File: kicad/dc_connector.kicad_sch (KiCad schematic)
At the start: 8 parts

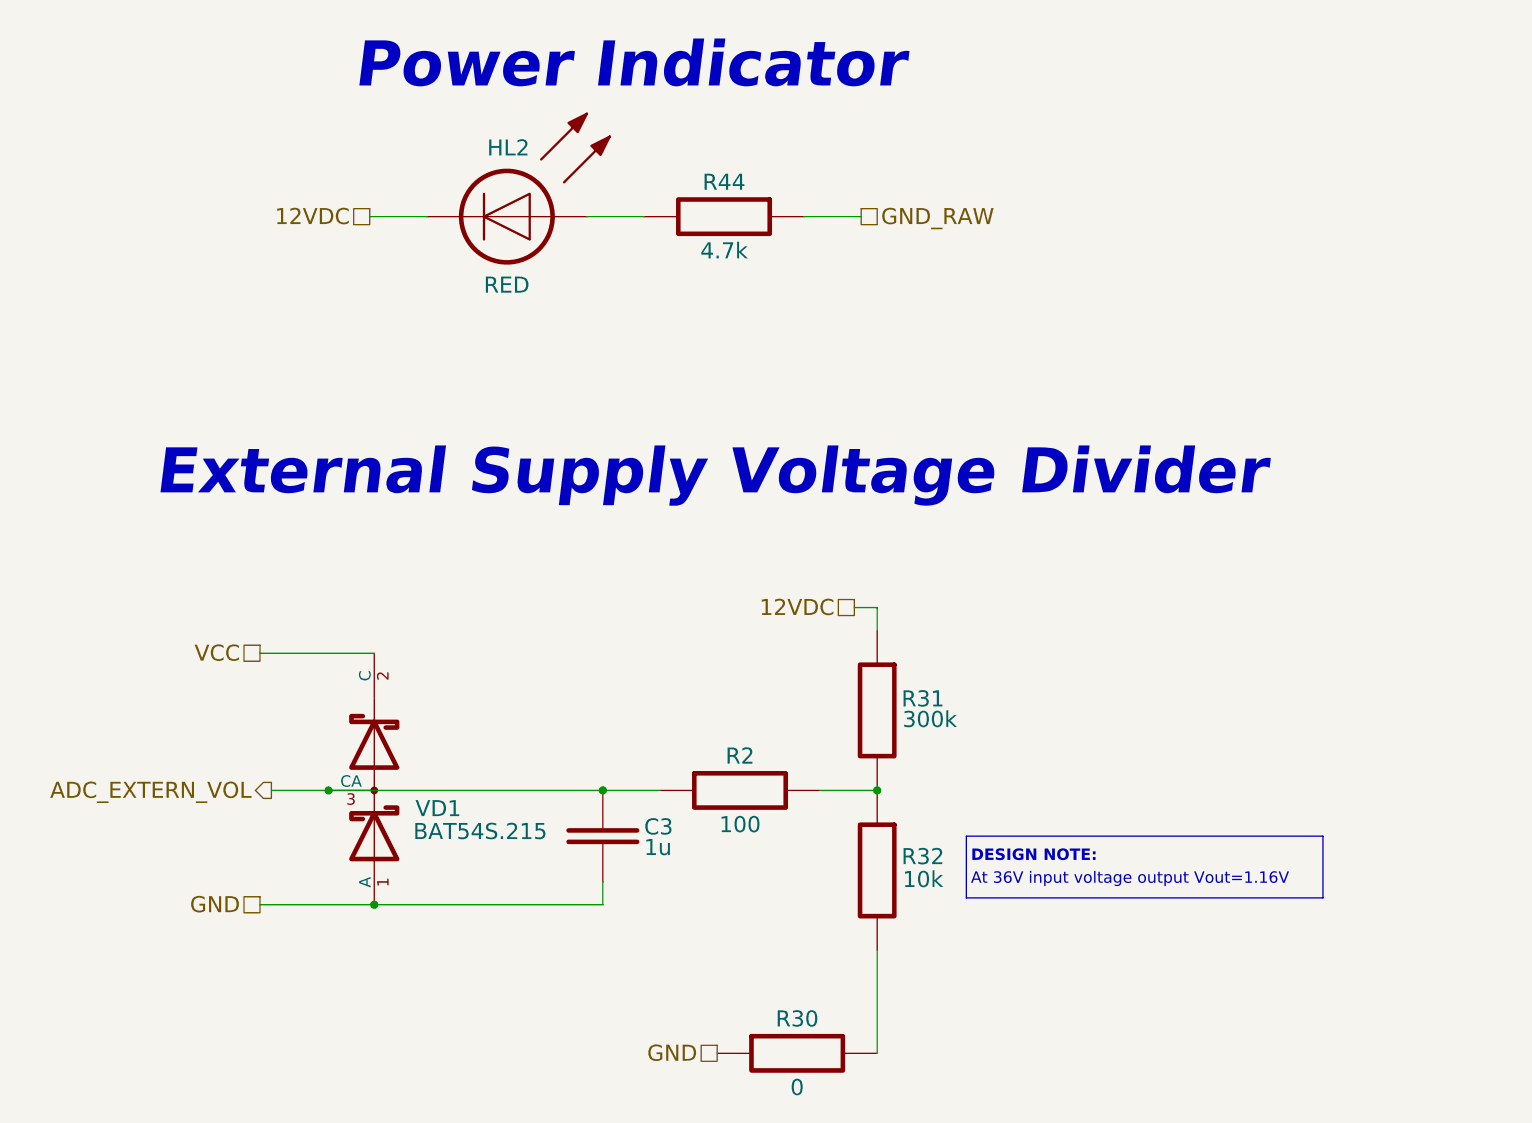
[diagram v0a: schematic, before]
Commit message: Reannotate schematic; Fix 5032 crystal footprint field; Update PCB with 5032 crystal
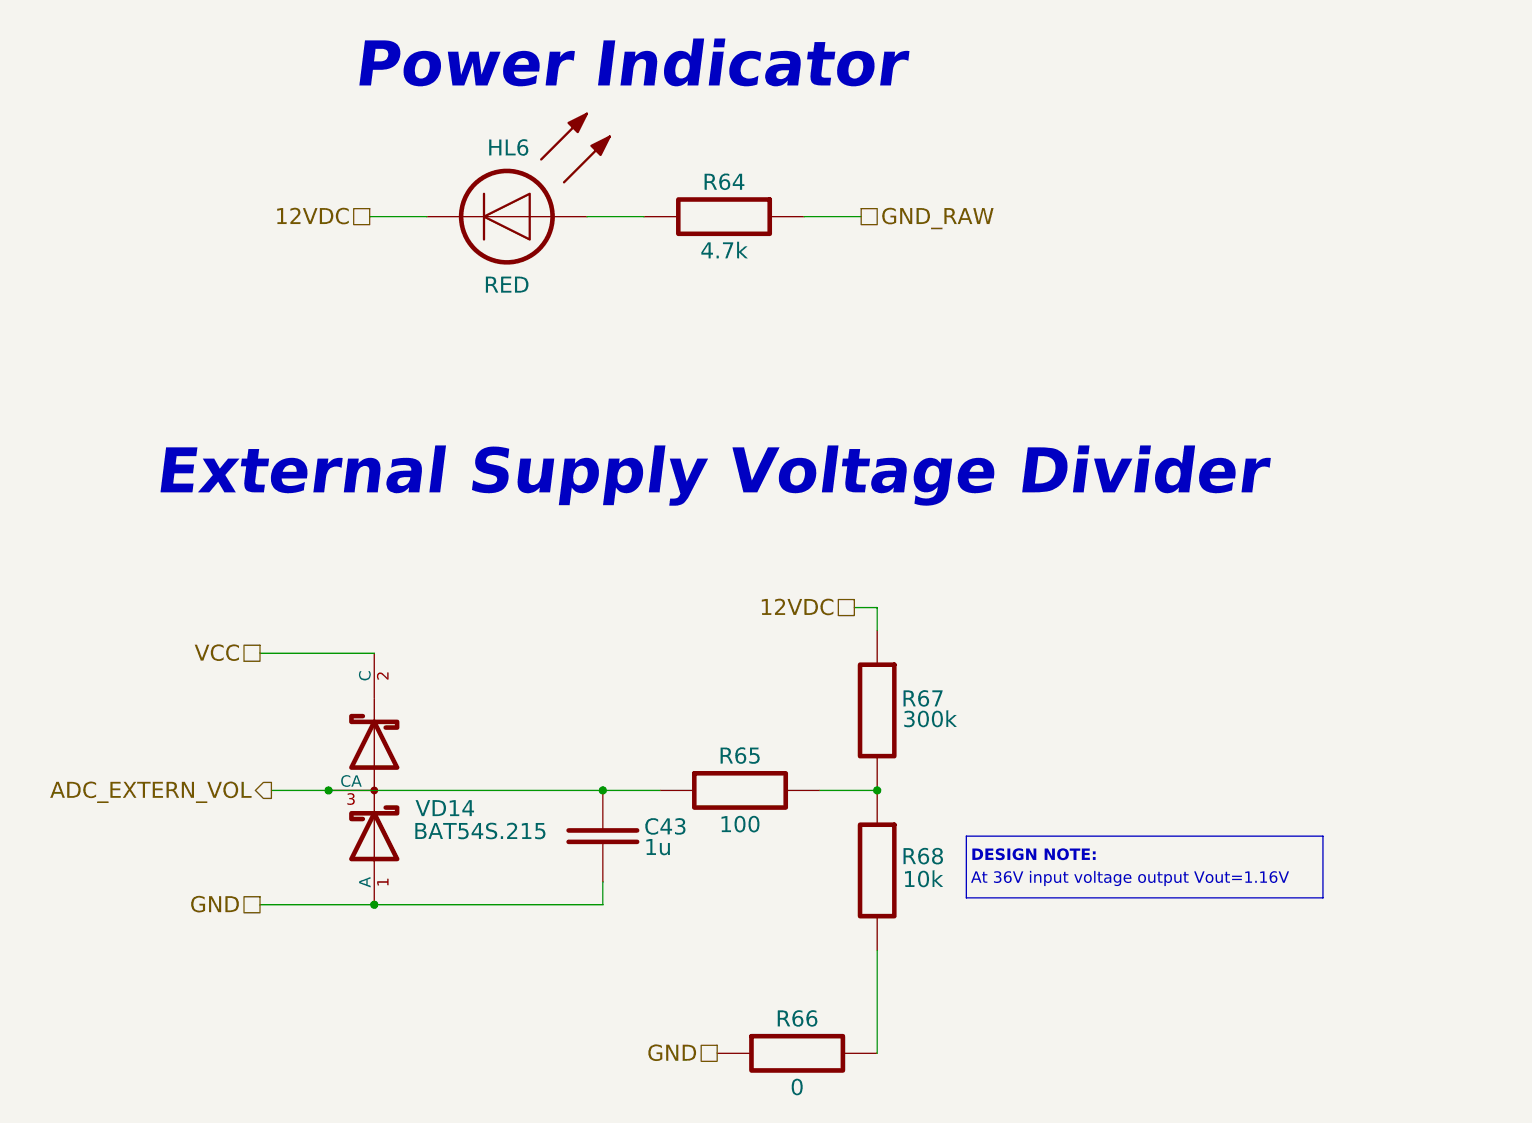
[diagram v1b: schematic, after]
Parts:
- renumbered C3 to C43, HL2 to HL6, R44 to R64, R2 to R65, R30 to R66, R31 to R67, R32 to R68, VD1 to VD14
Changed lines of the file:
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@@
   (symbol (lib_id "Resistors:R_RES") (at 166.37 122.174 0) (unit 1)
     (in_bom yes) (on_board yes)
-    (property "Reference" "R2" (id 0) (at 166.37 118.364 0)
+    (property "Reference" "R65" (id 0) (at 166.37 118.364 0)
       (effects (font (size 1.778 1.778)))
     )
@@
   (symbol (lib_id "Resistors:R_RES") (at 172.72 151.384 0) (unit 1)
     (in_bom yes) (on_board yes)
-    (property "Reference" "R30" (id 0) (at 172.72 147.574 0)
+    (property "Reference" "R66" (id 0) (at 172.72 147.574 0)
       (effects (font (size 1.778 1.778)))
     )
@@
   (symbol (lib_id "Resistors:R_RES") (at 164.592 58.42 0) (mirror y) (unit 1)
     (in_bom yes) (on_board yes)
-    (property "Reference" "R44" (id 0) (at 164.592 54.61 0)
+    (property "Reference" "R64" (id 0) (at 164.592 54.61 0)
       (effects (font (size 1.778 1.778)))
     )
@@
   (symbol (lib_id "Diodes:VD_SCHOTTKY_PROTECT") (at 125.73 122.174 0) (unit 1)
     (in_bom yes) (on_board yes)
-    (property "Reference" "VD1" (id 0) (at 130.302 124.206 0)
+    (property "Reference" "VD14" (id 0) (at 130.302 124.206 0)
       (effects (font (size 1.778 1.778)) (justify left))
     )
@@
   (symbol (lib_id "Diodes:HL_LED") (at 140.462 58.42 0) (mirror y) (unit 1)
     (in_bom yes) (on_board yes)
-    (property "Reference" "HL2" (id 0) (at 143.002 50.8 0)
+    (property "Reference" "HL6" (id 0) (at 143.002 50.8 0)
       (effects (font (size 1.778 1.778)) (justify left))
     )
@@
   (symbol (lib_id "Resistors:R_RES") (at 181.61 113.284 270) (unit 1)
     (in_bom yes) (on_board yes)
-    (property "Reference" "R31" (id 0) (at 186.69 112.014 90)
+    (property "Reference" "R67" (id 0) (at 186.69 112.014 90)
       (effects (font (size 1.778 1.778)))
     )
@@
   (symbol (lib_id "Capacitors:C_CAP") (at 151.13 127.254 270) (unit 1)
     (in_bom yes) (on_board yes)
-    (property "Reference" "C3" (id 0) (at 155.702 126.238 90)
+    (property "Reference" "C43" (id 0) (at 155.702 126.238 90)
       (effects (font (size 1.778 1.778)) (justify left))
     )
@@
   (symbol (lib_id "Resistors:R_RES") (at 181.61 131.064 270) (unit 1)
     (in_bom yes) (on_board yes)
-    (property "Reference" "R32" (id 0) (at 186.69 129.54 90)
+    (property "Reference" "R68" (id 0) (at 186.69 129.54 90)
       (effects (font (size 1.778 1.778)))
     )

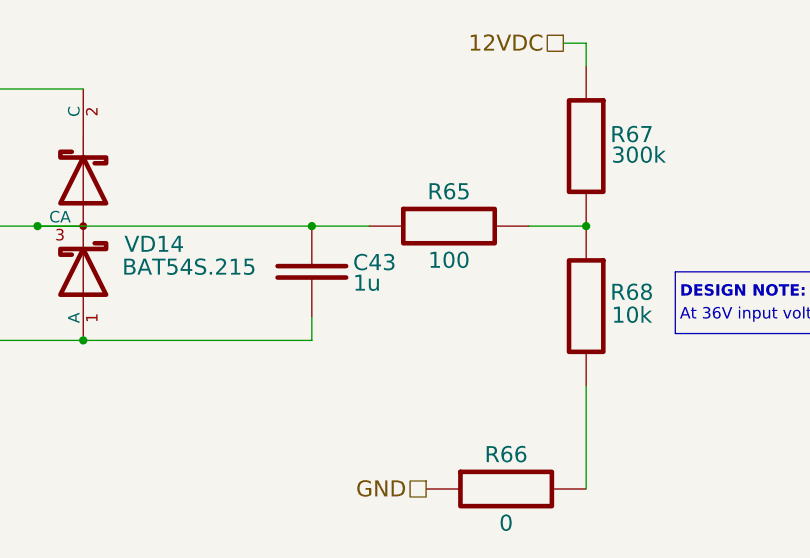
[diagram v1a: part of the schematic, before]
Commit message: Add voltage value to caps, update BOM, SCH, ASM
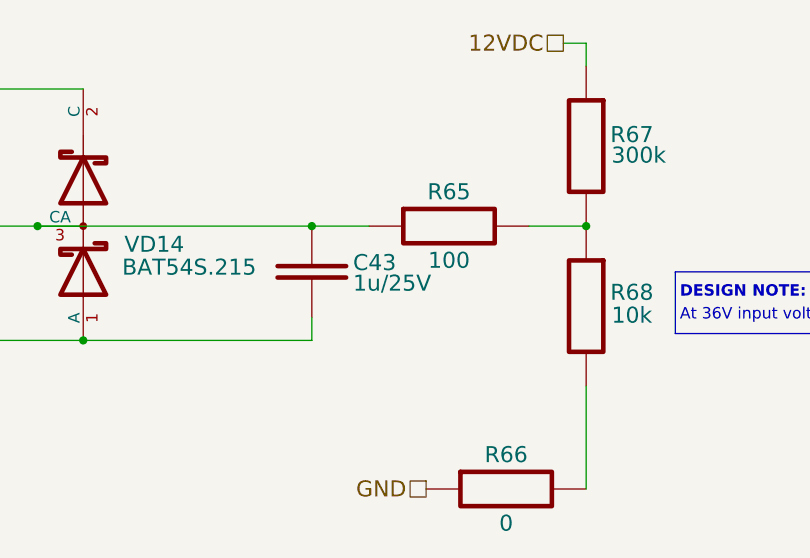
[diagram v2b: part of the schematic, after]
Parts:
- C43: value 1u -> 1u/25V; Case/Package (none) -> 0603; Tolerance (none) -> ±10%; Type (none) -> X7R
- R64, R65, R66, R67, R68: Case/Package 0000 -> 0603; Tolerance ±% -> ±5%
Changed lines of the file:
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@@
     (effects (font (size 1.778 1.778)) (justify right))
   )
-  (symbol (lib_id "Resistors:R_RES") (at 166.37 122.174 0) (unit 1)
+  (symbol (lib_name "R_RES_3") (lib_id "Resistors:R_RES") (at 166.37 122.174 0) (unit 1)
     (in_bom yes) (on_board yes)
     (property "Reference" "R65" (id 0) (at 166.37 118.364 0)
@@
       (effects (font (size 1.778 1.778)))
     )
-    (property "Case/Package" "0000" (id 5) (at 166.37 128.524 0)
+    (property "Case/Package" "0603" (id 5) (at 166.37 128.524 0)
       (effects (font (size 1.27 1.27)) hide)
     )
@@
       (effects (font (size 1.27 1.27)) hide)
     )
-    (property "Tolerance" "±%" (id 7) (at 166.37 131.826 0)
-      (effects (font (size 1.27 1.27)) hide)
-    )
-    (pin "1")
-    (pin "2")
-  )
-  (symbol (lib_id "Resistors:R_RES") (at 172.72 151.384 0) (unit 1)
+    (property "Tolerance" "±5%" (id 7) (at 166.37 131.826 0)
+      (effects (font (size 1.27 1.27)) hide)
+    )
+    (property "Part Number" "" (id 8) (at 166.37 122.174 0))
+    (pin "1")
+    (pin "2")
+  )
+  (symbol (lib_name "R_RES_2") (lib_id "Resistors:R_RES") (at 172.72 151.384 0) (unit 1)
     (in_bom yes) (on_board yes)
     (property "Reference" "R66" (id 0) (at 172.72 147.574 0)
@@
       (effects (font (size 1.778 1.778)))
     )
-    (property "Case/Package" "0000" (id 5) (at 172.72 157.734 0)
+    (property "Case/Package" "0603" (id 5) (at 172.72 157.734 0)
       (effects (font (size 1.27 1.27)) hide)
     )
@@
       (effects (font (size 1.27 1.27)) hide)
     )
-    (property "Tolerance" "±%" (id 7) (at 172.72 161.036 0)
-      (effects (font (size 1.27 1.27)) hide)
-    )
+    (property "Tolerance" "±5%" (id 7) (at 172.72 161.036 0)
+      (effects (font (size 1.27 1.27)) hide)
+    )
+    (property "Part Number" "" (id 8) (at 172.72 151.384 0))
     (pin "1")
     (pin "2")
@@
       (effects (font (size 1.778 1.778)))
     )
-    (property "Case/Package" "0000" (id 5) (at 164.592 64.77 0)
+    (property "Case/Package" "0603" (id 5) (at 164.592 64.77 0)
       (effects (font (size 1.27 1.27)) hide)
     )
@@
       (effects (font (size 1.27 1.27)) hide)
     )
-    (property "Tolerance" "±%" (id 7) (at 164.592 68.072 0)
-      (effects (font (size 1.27 1.27)) hide)
-    )
+    (property "Tolerance" "±5%" (id 7) (at 164.592 68.072 0)
+      (effects (font (size 1.27 1.27)) hide)
+    )
+    (property "Part Number" "" (id 8) (at 164.592 58.42 0))
     (pin "1")
     (pin "2")
@@
     (pin "2")
   )
-  (symbol (lib_id "Resistors:R_RES") (at 181.61 113.284 270) (unit 1)
+  (symbol (lib_name "R_RES_4") (lib_id "Resistors:R_RES") (at 181.61 113.284 270) (unit 1)
     (in_bom yes) (on_board yes)
     (property "Reference" "R67" (id 0) (at 186.69 112.014 90)
@@
       (effects (font (size 1.778 1.778)))
     )
-    (property "Case/Package" "0000" (id 5) (at 175.26 113.284 0)
+    (property "Case/Package" "0603" (id 5) (at 175.26 113.284 0)
       (effects (font (size 1.27 1.27)) hide)
     )
@@
       (effects (font (size 1.27 1.27)) hide)
     )
-    (property "Tolerance" "±%" (id 7) (at 171.958 113.284 0)
-      (effects (font (size 1.27 1.27)) hide)
-    )
+    (property "Tolerance" "±5%" (id 7) (at 171.958 113.284 0)
+      (effects (font (size 1.27 1.27)) hide)
+    )
+    (property "Part Number" "" (id 8) (at 181.61 113.284 0))
     (pin "1")
     (pin "2")
@@
       (effects (font (size 1.778 1.778)) (justify left))
     )
-    (property "Value" "1u" (id 1) (at 155.702 128.524 90)
+    (property "Value" "1u/25V" (id 1) (at 155.702 128.524 90)
       (effects (font (size 1.778 1.778)) (justify left))
     )
@@
       (effects (font (size 1.778 1.778)))
     )
-    (pin "1")
-    (pin "2")
-  )
-  (symbol (lib_id "Resistors:R_RES") (at 181.61 131.064 270) (unit 1)
+    (property "Voltage" "" (id 5) (at 151.13 127.254 0)
+      (effects (font (size 1.27 1.27)) hide)
+    )
+    (property "Case/Package" "0603" (id 6) (at 151.13 127.254 0)
+      (effects (font (size 1.27 1.27)) hide)
+    )
+    (property "Type" "X7R" (id 7) (at 140.97 127.254 0)
+      (effects (font (size 1.27 1.27)) hide)
+    )
+    (property "Tolerance" "±10%" (id 8) (at 138.43 127.254 0)
+      (effects (font (size 1.27 1.27)) hide)
+    )
+    (pin "1")
+    (pin "2")
+  )
+  (symbol (lib_name "R_RES_1") (lib_id "Resistors:R_RES") (at 181.61 131.064 270) (unit 1)
     (in_bom yes) (on_board yes)
     (property "Reference" "R68" (id 0) (at 186.69 129.54 90)
@@
       (effects (font (size 1.778 1.778)))
     )
-    (property "Case/Package" "0000" (id 5) (at 175.26 131.064 0)
+    (property "Case/Package" "0603" (id 5) (at 175.26 131.064 0)
       (effects (font (size 1.27 1.27)) hide)
     )
@@
       (effects (font (size 1.27 1.27)) hide)
     )
-    (property "Tolerance" "±%" (id 7) (at 171.958 131.064 0)
-      (effects (font (size 1.27 1.27)) hide)
-    )
-    (pin "1")
-    (pin "2")
+    (property "Tolerance" "±5%" (id 7) (at 171.958 131.064 0)
+      (effects (font (size 1.27 1.27)) hide)
+    )
+    (property "Part Number" "" (id 8) (at 181.61 131.064 0))
+    (pin "1")
+    (pin "2")

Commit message: Add wiring diagram; Add work ours (stage 2); refactor folders
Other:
- title: (none) -> RadioSens v1
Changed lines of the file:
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@@
 (kicad_sch (version 20211123) (generator eeschema)
   (paper "A4")
+  (title_block
+    (title "RadioSens v1")
+    (comment 2 "Electrical Circuit")
+  )
   (junction (at 181.61 122.174) (diameter 0) (color 0 0 0 0)
   )
